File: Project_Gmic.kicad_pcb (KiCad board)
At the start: 2 copper layers, 55.9 x 62.2 mm, 54 parts, among them J1 USB4085-GF-A, J2 SJ1-3523N, SW1 PCM12SMTR, U1 AD8532, U2 AD8532, U3 AD8532, U4 AD8531, U5 TC1055

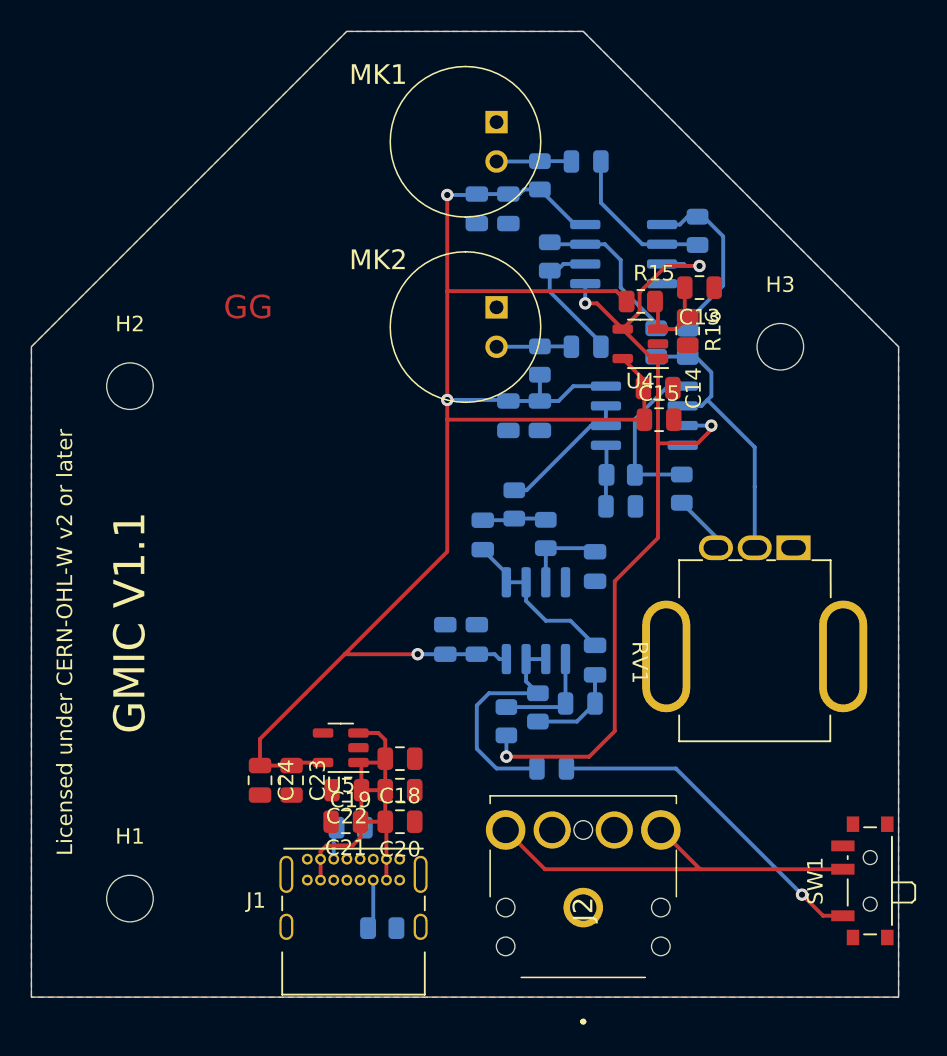
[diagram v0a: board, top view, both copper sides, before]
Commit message: fixing pcb error, reset footprints from libs, add diode
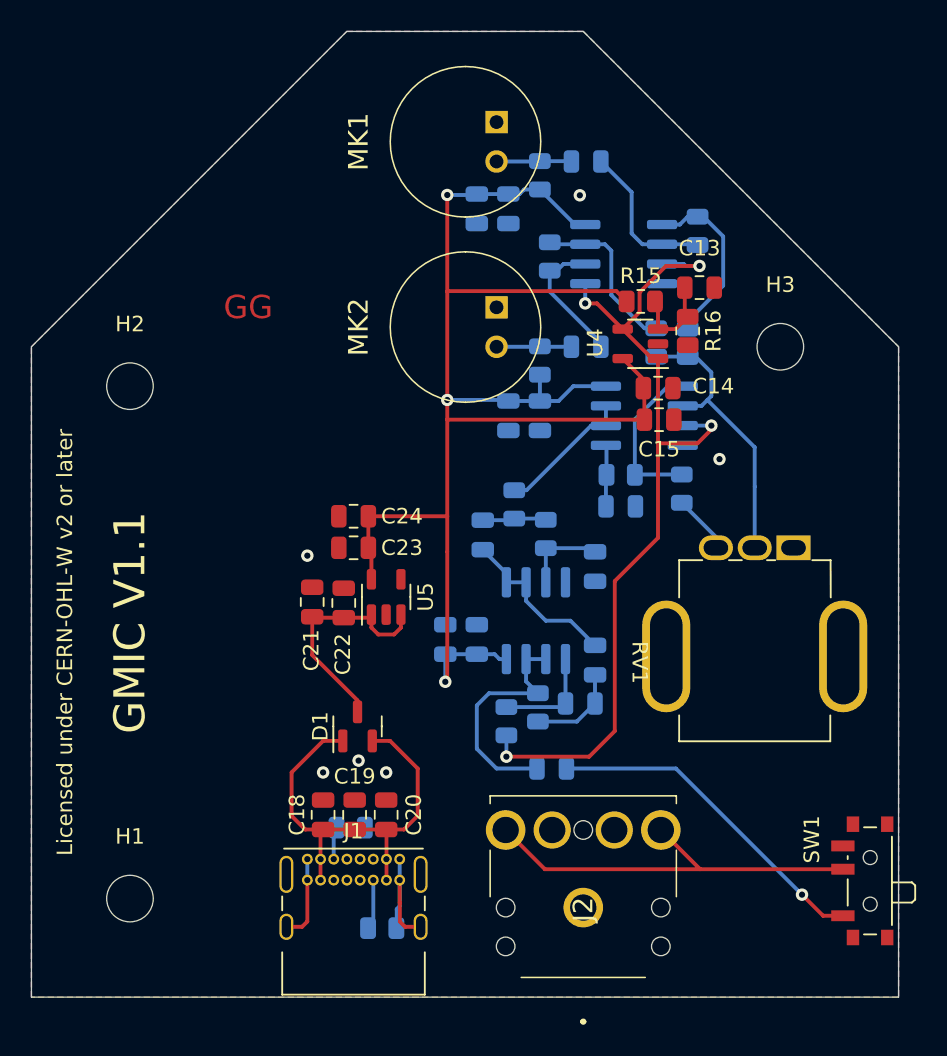
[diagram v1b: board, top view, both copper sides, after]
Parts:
- added D1: BAT54C, Package_TO_SOT_SMD:SOT-23, F.Cu at (69.3, 136.2)
- moved C24 18.1 mm to (69.0, 122.7), turned to 180 degrees
- moved C23 15.5 mm to (69.0, 124.7), turned to 180 degrees
- moved C21 14.3 mm to (66.4, 128.2), turned to 90 degrees
- moved C22 12.1 mm to (68.4, 128.3), turned to 90 degrees
- moved U5 10.1 mm to (71.1, 127.9), turned to 90 degrees
- moved C18 6.13 mm to (67.1, 141.9), turned to 90 degrees
- moved C19 3.32 mm to (69.1, 141.9), turned to 90 degrees
- moved C20 1.00 mm to (71.1, 141.9), turned to 90 degrees
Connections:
- C21 pad 1: +5V -> VCC
- C22 pad 1: +5V -> VCC
- U5 pad 1: +5V -> VCC
- U5 pad 3: +5V -> VCC
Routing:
- net VCC: track 0.00 -> 15.2 mm
- net GNDA: track 0.00 -> 14.2 mm, vias 0 -> 6
- net +3.3V: track 107.8 -> 97.9 mm
- net +5V: track 25.7 -> 29.1 mm

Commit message: finishing PCB, fix serigraph, complete BOM, fix some non-sense in footprints
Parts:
- moved RV1 14.4 mm to (97.4, 124.8)
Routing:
- net GNDA: track 14.2 -> 16.1 mm

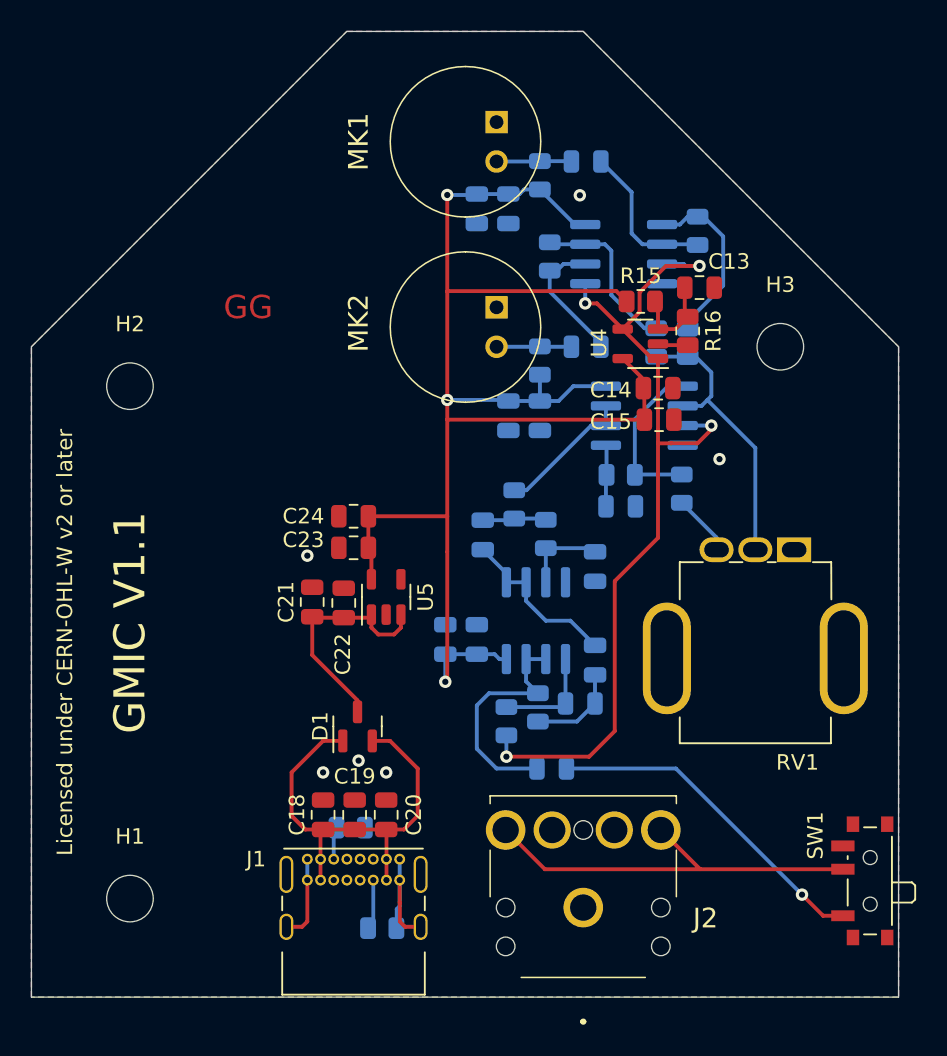
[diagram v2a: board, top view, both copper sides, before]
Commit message: moving mounting holes, fixing POT footprint, exporting fabrication files
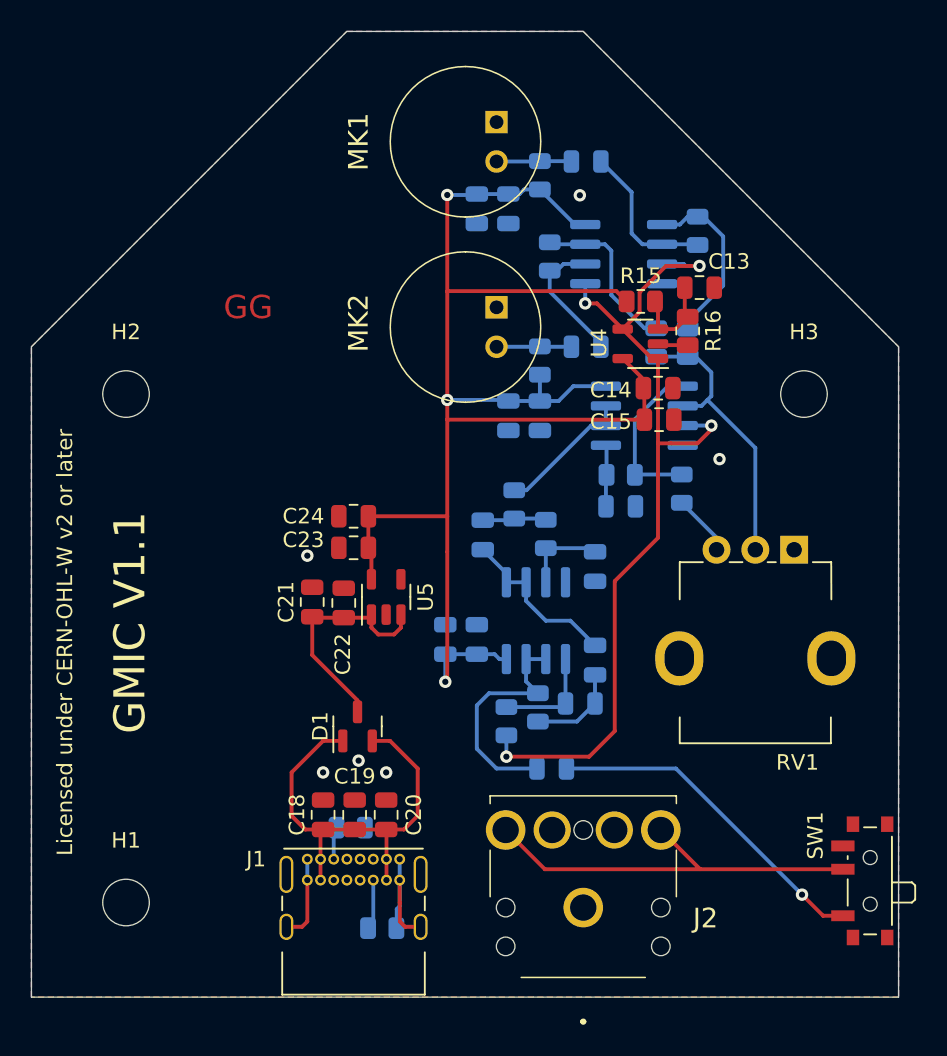
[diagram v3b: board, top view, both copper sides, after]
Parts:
- moved H3 3.41 mm to (98.0, 114.8)
- moved H2 0.57 mm to (54.4, 114.8)
- moved H1 0.36 mm to (54.4, 147.6)
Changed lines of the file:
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@@
     (fp_circle (center 7.5 2.5) (end 7.5 -1)
       (stroke (width 0.1) (type solid)) (fill none) (layer "F.Fab"))
-    (pad "" thru_hole oval (at 7 -3.2) (size 3.1 7.2) (drill oval 2.1 6.2) (layers "*.Cu" "*.Mask"))
-    (pad "" thru_hole oval (at 7 8.2) (size 3.1 7.2) (drill oval 2.1 6.2) (layers "*.Cu" "*.Mask"))
-    (pad "1" thru_hole rect (at 0 0) (size 2.2 1.6) (drill oval 1.6 1) (layers "*.Cu" "*.Mask")
+    (pad "" thru_hole oval (at 7 -2.4) (size 3.1 3.5) (drill oval 1.9 2.3) (layers "*.Cu" "*.Mask"))
+    (pad "" thru_hole oval (at 7 7.4) (size 3.1 3.5) (drill oval 1.9 2.3) (layers "*.Cu" "*.Mask"))
+    (pad "1" thru_hole rect (at 0 0) (size 1.8 1.8) (drill 1) (layers "*.Cu" "*.Mask")
       (net 35 "unconnected-(RV1-Pad1)") (pinfunction "1") (pintype "passive+no_connect"))
-    (pad "2" thru_hole oval (at 0 2.5) (size 2.2 1.6) (drill oval 1.6 1) (layers "*.Cu" "*.Mask")
+    (pad "2" thru_hole oval (at 0 2.5) (size 1.8 1.8) (drill 1) (layers "*.Cu" "*.Mask")
       (net 32 "Net-(U2A--)") (pinfunction "2") (pintype "passive"))
-    (pad "3" thru_hole oval (at 0 5) (size 2.2 1.6) (drill oval 1.6 1) (layers "*.Cu" "*.Mask")
+    (pad "3" thru_hole oval (at 0 5) (size 1.8 1.8) (drill 1) (layers "*.Cu" "*.Mask")
       (net 34 "Net-(R14-Pad2)") (pinfunction "3") (pintype "passive"))
   )
   (footprint "MountingHole:MountingHole_3mm" (layer "F.Cu")
-    (at 54.61 147.32)
+    (at 54.356 147.574)
     (descr "Mounting Hole 3mm, no annular")
     (tags "mounting hole 3mm no annular")
@@
   )
   (footprint "MountingHole:MountingHole_3mm" (layer "F.Cu")
-    (at 54.61 114.3)
+    (at 54.356 114.808)
     (descr "Mounting Hole 3mm, no annular")
     (tags "mounting hole 3mm no annular")
@@
   )
   (footprint "MountingHole:MountingHole_3mm" (layer "F.Cu")
-    (at 96.52 111.76)
+    (at 98.044 114.808)
     (descr "Mounting Hole 3mm, no annular")
     (tags "mounting hole 3mm no annular")

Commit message: placement, BOM inside kicad
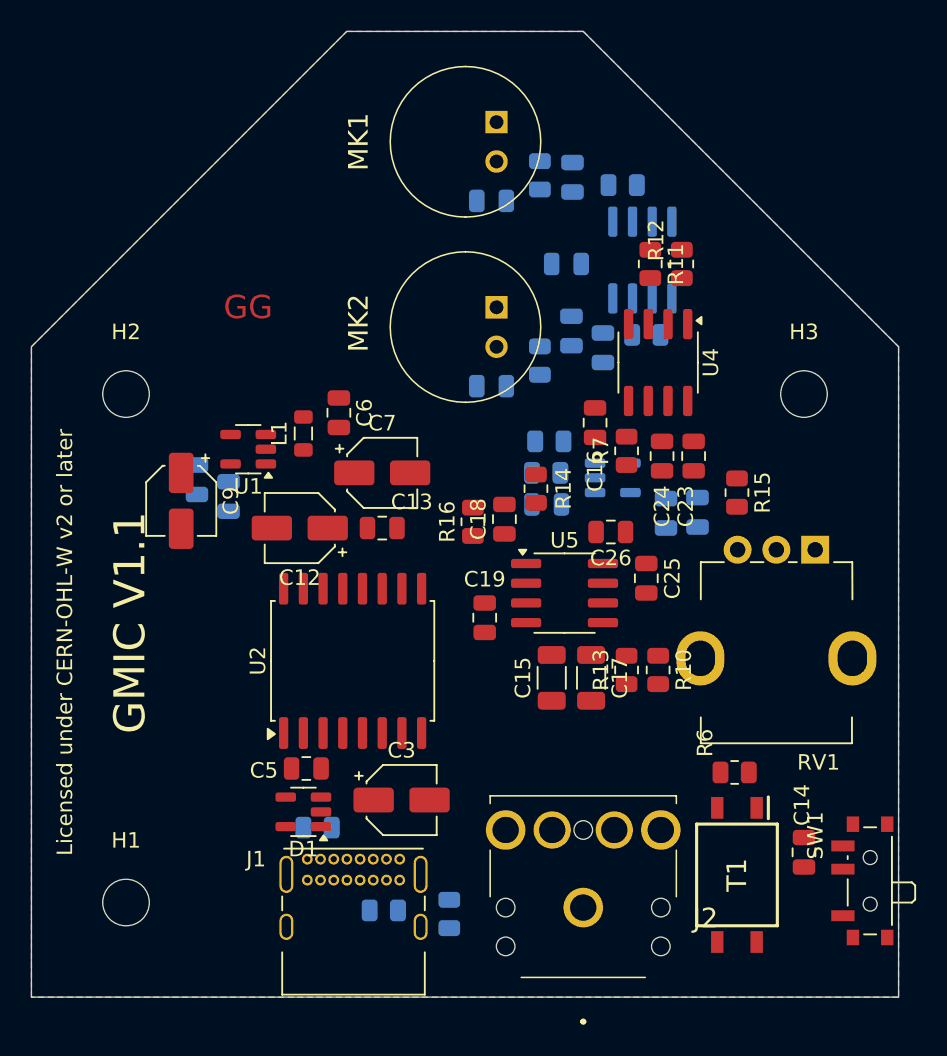
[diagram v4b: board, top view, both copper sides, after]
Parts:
- added C25: 100nF 16V X7R, Capacitor_SMD:C_0805_2012Metric, F.Cu at (87.9, 126.7)
- added C26: 1uF 16V X7R, Capacitor_SMD:C_0805_2012Metric, F.Cu at (85.6, 123.7)
- added C27: 100nF 16V X7R, Capacitor_SMD:C_0805_2012Metric, B.Cu at (89.2, 122.5)
- added C28: 1uF 16V X7R, Capacitor_SMD:C_0805_2012Metric, B.Cu at (91.2, 122.4)
- added L1: BLM21PG331SN1D, Inductor_SMD:L_0805_2012Metric, F.Cu at (65.8, 117.3)
- added R17: 10k, Resistor_SMD:R_0805_2012Metric, B.Cu at (81.6, 117.9)
- added R18: 10k, Resistor_SMD:R_0805_2012Metric, B.Cu at (81.4, 119.9)
- added T1: ESMIT-4180/C, SOP254P914X350:SOP254P914X350-4N, F.Cu at (93.7, 145.8)
- added U6: AD8531, Package_TO_SOT_SMD:SOT-23-5, B.Cu at (85.7, 120.2)
- C1, C2: value 2.2uF -> 2.2uF 16V X7R
- C10, C24: value 100nF -> 1uF 16V X7R
- C11, C23: value 1uF -> 100nF 16V X7R
- C12: value 2.2uF -> 10uF 16V; footprint Capacitor_SMD:C_0805_2012Metric -> Capacitor_SMD:CP_Elec_4x5.4; moved to F.Cu
- C13: value 2.2uF -> 100nF 16V X7R
- C14: value 100nF -> 2.2uF 16V X7R
- C15: value 1uF -> 100nF; footprint Capacitor_SMD:C_0805_2012Metric -> Capacitor_SMD:C_1206_3216Metric
- C16: value 100nF -> 100pF; moved to F.Cu
- C17: value 1uF -> 100nF; footprint Capacitor_SMD:C_0805_2012Metric -> Capacitor_SMD:C_1206_3216Metric; moved to F.Cu
- C18: value 100nF -> 100pF
- C19: value 1uF -> 100pF
- C20: value 2.2uF -> 2.2uF 16V X7R; moved to B.Cu
- C21: value 100nF -> 100nF 16V X7R; moved to B.Cu
- C22: value 1uF -> 1uF 16V X7R; moved to B.Cu
- C3: value 100nF -> 10uF 16V; footprint Capacitor_SMD:C_0805_2012Metric -> Capacitor_SMD:CP_Elec_4x5.4; moved to F.Cu
- C4, C8: value 100pF -> 100nF 16V X7R
- C5: value 100nF -> 100nF 16V X7R; moved to F.Cu
- C6: value 100pF -> 100nF 16V X7R; moved to F.Cu
- C7: value 100nF -> 1uF 16V; footprint Capacitor_SMD:C_0805_2012Metric -> Capacitor_SMD:CP_Elec_4x5.4; moved to F.Cu
- C9: value 1uF -> 1uF 16V; footprint Capacitor_SMD:C_0805_2012Metric -> Capacitor_SMD:CP_Elec_4x5.4; moved to F.Cu
- D1: footprint Package_TO_SOT_SMD:SOT-23 -> Package_TO_SOT_SMD:SOT-23-5
- R10: value 100k -> 80k; moved to F.Cu
- R11, R13, R7: moved to F.Cu
- R12: value 80k -> 100k; moved to F.Cu
- R14: value 50k -> 80k; moved to F.Cu
- R15: value 10k -> 50k
- R16: value 10k -> 80k
- R2: value 5.1k -> 0
- R5: value 80k -> 5.1k
- R6: value 80k -> 50 1-5%; moved to F.Cu
- U1: value AD8532 -> TC1055; footprint Package_SO:SOIC-8_3.9x4.9mm_P1.27mm -> Package_TO_SOT_SMD:SOT-23-5; moved to F.Cu
- U2: value AD8532 -> R05CTE05S; footprint Package_SO:SOIC-8_3.9x4.9mm_P1.27mm -> Package_SO:SOIC-16W_7.5x10.3mm_P1.27mm; moved to F.Cu
- U4: value AD8531 -> AD8532; footprint Package_TO_SOT_SMD:SOT-23-5 -> Package_SO:SOIC-8_3.9x4.9mm_P1.27mm
- U5: value TC1055 -> AD8532; footprint Package_TO_SOT_SMD:SOT-23-5 -> Package_SO:SOIC-8_3.9x4.9mm_P1.27mm
- moved C14 31.4 mm to (98.0, 144.3), turned to -90 degrees
- moved R5 30.0 mm to (66.7, 142.7), turned to 180 degrees
- moved U1 27.3 mm to (62.2, 118.4)
- moved C9 26.8 mm to (57.9, 121.7)
- moved C22 26.1 mm to (82.7, 106.4), turned to 180 degrees
- moved C13 25.7 mm to (70.9, 123.4)
- moved C21 24.9 mm to (85.1, 111.8), turned to -90 degrees
- moved U2 24.6 mm to (69.0, 132.0), turned to 90 degrees
- moved U3 24.2 mm to (87.6, 106.2)
- moved C23 22.7 mm to (90.9, 118.8), turned to -90 degrees
- moved C20 22.5 mm to (81.5, 121.9), turned to 180 degrees
- moved C10 22.5 mm to (58.9, 120.3)
- moved C12 22.4 mm to (65.6, 123.4)
- moved C18 22.3 mm to (78.7, 122.9)
- moved C4 21.4 mm to (77.9, 102.4)
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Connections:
- C12 pad 1: /AUDIO_OUT -> VCC
- C12 pad 2: /AUDIO_PASS_HIGH -> GND
- C13 pad 1: Net-(U4-+) -> VCC
- C13 pad 2: GNDA -> GND
- C14 pad 1: +3.3V -> Net-(T1-AA)
- C14 pad 2: GNDA -> Net-(SW1-B)
- C15 pad 1: +3.3V -> Net-(C15-Pad1)
- C15 pad 2: GNDA -> /FilteringAndAmplification/AUDIO_PASS_LOW
- C16 pad 1: +3.3V -> GNDA
- C16 pad 2: GNDA -> Net-(U4B-+)
- C17 pad 1: +3.3V -> Net-(U5B-+)
- C17 pad 2: GNDA -> Net-(C15-Pad1)
- C18 pad 1: +5V -> /FilteringAndAmplification/AUDIO_PASS_LOW
- C18 pad 2: GNDA -> Net-(C18-Pad2)
- C19 pad 1: +5V -> GNDA
- C19 pad 2: GNDA -> Net-(U5A-+)
- C20 pad 1: +5V -> Net-(U6-+)
- C21 pad 1: VCC -> +3.3V
- C22 pad 1: VCC -> +3.3V
- C3 pad 1: Net-(C3-Pad1) -> +5V
- C3 pad 2: /AUDIO_PASS_LOW -> GNDPWR
- C4 pad 1: GNDA -> +3.3V
- C4 pad 2: Net-(U2B-+) -> GNDA
- C5 pad 1: Net-(U3B-+) -> +5V
- C5 pad 2: Net-(C3-Pad1) -> GNDPWR
- C6 pad 1: /AUDIO_PASS_LOW -> VCC
- C6 pad 2: Net-(C6-Pad2) -> GND
- C7 pad 1: +3.3V -> VCC
- C7 pad 2: GNDA -> GND
- C8 pad 1: GNDA -> +3.3V
- C8 pad 2: Net-(U3A-+) -> GNDA
- D1 pad 1: +5V -> Net-(D1-Pad1)
- D1 pad 2: +5V -> Net-(D1-Pad1)
- D1 pad 3: VCC -> +5V
- J1 pad A1: GNDA -> GNDPWR
- J1 pad A12: GNDA -> GNDPWR
- J1 pad A4: +5V -> Net-(D1-Pad1)
- J1 pad A9: +5V -> Net-(D1-Pad1)
- J1 pad B1: GNDA -> GNDPWR
- J1 pad B12: GNDA -> GNDPWR
- J1 pad B4: +5V -> Net-(D1-Pad1)
- J1 pad B9: +5V -> Net-(D1-Pad1)
- J1 pad S1: GNDA -> Net-(J1-SHIELD)
- J2 pad 1: GNDA -> Net-(T1-SA)
- J2 pad 2: Net-(SW1-B) -> Net-(T1-SB)
- J2 pad 3: Net-(SW1-B) -> Net-(T1-SB)
- R10 pad 1: Net-(U2A--) -> /AUDIO_READY
- R10 pad 2: Net-(R10-Pad2) -> Net-(C15-Pad1)
- R11 pad 1: Net-(U2A--) -> Net-(U4A--)
- R12 pad 1: Net-(C6-Pad2) -> Net-(U4A--)
- R12 pad 2: Net-(U2B--) -> Net-(R12-Pad2)
- R13 pad 1: Net-(U3A-+) -> /FilteringAndAmplification/V_OFFSET
- R13 pad 2: Net-(C6-Pad2) -> Net-(U5B-+)
- R14 pad 1: /AUDIO_AVERAGE -> Net-(C18-Pad2)
- R14 pad 2: Net-(R14-Pad2) -> Net-(U4B--)
- R15 pad 1: +3.3V -> /FilteringAndAmplification/AUDIO_AVERAGE
- R15 pad 2: Net-(U4-+) -> Net-(R15-Pad2)
- R16 pad 1: Net-(U4-+) -> Net-(U5A-+)
- R16 pad 2: GNDA -> Net-(C18-Pad2)
- R2 pad 1: Net-(J1-CC2) -> GNDPWR
- R2 pad 2: GNDA -> Net-(J1-SHIELD)
- R4 pad 1: Net-(J1-CC1) -> Net-(J1-CC2)
- R4 pad 2: GNDA -> GNDPWR
- R5 pad 1: Net-(U2B-+) -> Net-(J1-CC1)
- R5 pad 2: /AUDIO_AVERAGE -> GNDPWR
- R6 pad 1: /AUDIO_PASS_HIGH -> GNDA
- R6 pad 2: Net-(C3-Pad1) -> Net-(T1-AB)
- R7 pad 1: /V_OFFSET -> Net-(U4B-+)
- R7 pad 2: Net-(U3B-+) -> /FilteringAndAmplification/AUDIO_AVERAGE
- R8 pad 1: Net-(R10-Pad2) -> Net-(R11-Pad2)
- R9 pad 1: Net-(R11-Pad2) -> Net-(R12-Pad2)
- RV1 pad 2: Net-(U2A--) -> Net-(U4A--)
- RV1 pad 3: Net-(R14-Pad2) -> Net-(R15-Pad2)
- SW1 pad 1: /AUDIO_OUT -> /AUDIO_READY
- SW1 pad 3: GNDA -> unconnected-(SW1-C-Pad3)
- U1 pad 1: Net-(R10-Pad2) -> VCC
- U1 pad 2: /AUDIO_1_IN -> GNDA
- U1 pad 3: /V_OFFSET -> VCC
- U1 pad 4: GNDA -> unconnected-(U1-~{ERROR}-Pad4)
- U1 pad 5: /V_OFFSET -> +3.3V
- U2 pad 1: /AUDIO_AVERAGE -> GNDPWR
- U2 pad 2: Net-(U2A--) -> GNDPWR
- U2 pad 3: /V_OFFSET -> +5V
- U2 pad 4: GNDA -> +5V
- U2 pad 5: Net-(U2B-+) -> GNDPWR
- U2 pad 6: Net-(U2B--) -> GNDPWR
- U2 pad 7: Net-(U2B--) -> GNDPWR
- U2 pad 8: +3.3V -> GNDPWR
- U3 pad 1: /AUDIO_PASS_LOW -> Net-(R11-Pad2)
- U3 pad 2: /AUDIO_PASS_LOW -> /AUDIO_1_IN
- U3 pad 3: Net-(U3A-+) -> /FilteringAndAmplification/V_OFFSET
- U3 pad 5: Net-(U3B-+) -> /FilteringAndAmplification/V_OFFSET
- U3 pad 6: /AUDIO_PASS_HIGH -> /AUDIO_2_IN
- U3 pad 7: /AUDIO_PASS_HIGH -> Net-(R12-Pad2)
- U4 pad 1: /V_OFFSET -> /FilteringAndAmplification/AUDIO_AVERAGE
- U4 pad 2: GNDA -> Net-(U4A--)
- U4 pad 3: Net-(U4-+) -> /FilteringAndAmplification/V_OFFSET
- U4 pad 4: /V_OFFSET -> GNDA
- U4 pad 5: +3.3V -> Net-(U4B-+)
- U5 pad 1: VCC -> /FilteringAndAmplification/AUDIO_PASS_LOW
- U5 pad 2: GNDA -> /FilteringAndAmplification/AUDIO_PASS_LOW
- U5 pad 3: VCC -> Net-(U5A-+)
- U5 pad 4: unconnected-(U5-~{ERROR}-Pad4) -> GNDA
- U5 pad 5: +3.3V -> Net-(U5B-+)
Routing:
- net +3.3V: track 97.9 -> 0.00 mm, vias 3 -> 0
- net /V_OFFSET: track 57.4 -> 0.00 mm, vias 4 -> 0
- net +5V: track 29.1 -> 0.00 mm
- net Net-(SW1-B): track 26.4 -> 0.00 mm
- net /AUDIO_OUT: track 21.7 -> 0.00 mm, vias 1 -> 0
- net Net-(U2A--): track 18.5 -> 0.00 mm
- net GNDA: track 16.1 -> 0.00 mm, vias 6 -> 0
- net /AUDIO_PASS_HIGH: track 15.2 -> 0.00 mm
- net VCC: track 15.2 -> 0.00 mm
- net Net-(R10-Pad2): track 11.6 -> 0.00 mm
- net /AUDIO_PASS_LOW: track 10.8 -> 0.00 mm
- net Net-(R11-Pad2): track 10.8 -> 0.00 mm
- net /AUDIO_AVERAGE: track 10.6 -> 0.00 mm
- net /AUDIO_1_IN: track 10.0 -> 0.00 mm
- net Net-(U2B--): track 8.90 -> 0.00 mm
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
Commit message: first step final
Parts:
- D1: footprint Package_TO_SOT_SMD:SOT-23-5 -> Package_TO_SOT_SMD:SOT-23
- moved D1 0.17 mm to (66.0, 141.7), turned to 90 degrees
- moved C5 0.16 mm to (66.0, 138.8)
- moved U2 0.14 mm to (69.0, 131.9)
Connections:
- net Net-(J1-SHIELD) renamed /USB_SHIELD
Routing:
- net +3.3V: track 0.00 -> 98.4 mm, vias 0 -> 5
- net /FilteringAndAmplification/V_OFFSET: track 0.00 -> 38.4 mm, vias 0 -> 2
- net /AUDIO_READY: track 0.00 -> 36.0 mm
- net VCC: track 0.00 -> 25.8 mm
- net Net-(U4A--): track 0.00 -> 25.2 mm
- net Net-(T1-SB): track 0.00 -> 22.4 mm
- net /FilteringAndAmplification/AUDIO_AVERAGE: track 0.00 -> 17.8 mm
- net GNDPWR: track 0.00 -> 16.1 mm, vias 0 -> 3
- net GNDA: track 0.00 -> 16.0 mm, vias 0 -> 61
- net Net-(D1-Pad1): track 0.00 -> 14.3 mm
- net +5V: track 0.00 -> 12.9 mm
- net Net-(U4B--): track 0.00 -> 11.9 mm
- net /AUDIO_2_IN: track 0.00 -> 10.1 mm
- net /FilteringAndAmplification/AUDIO_PASS_LOW: track 0.00 -> 9.63 mm
- net Net-(T1-SA): track 0.00 -> 9.56 mm
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- added copper zone on B.Cu, net /USB_SHIELD
- added copper zone on F.Cu, net GND
- added copper zone on F.Cu, net GNDPWR
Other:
- board text added: "GMIC V1.2"
- board text removed: "GMIC V1.1"
